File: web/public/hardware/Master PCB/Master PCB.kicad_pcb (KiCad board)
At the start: 2 copper layers, 104 parts, among them J1 SWD Conn, J10 LED3, J11 LDR4, J12 LED4, J13 LED Conn, J2 OLED1, J3 OLED2, J4 5V_IN, J5 LDR1, J6 LED1, J7 LDR2, J8 LED2, J9 LDR3, Q1 2N7000, Q2 2N7000, Q3 2N7000, Q4 2N7000, SW1 nRST, SW2 Menu Encoder, U1 STM32U585VITx, U2 M95P32-IXMNT, U3 TLV62568DBV, U4 LM339

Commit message: Route lots
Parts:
- added C21: 100nF, Capacitor_SMD:C_0805_2012Metric_Pad1.18x1.45mm_HandSolder, F.Cu at (163.5, 106.0)
- U4: footprint Package_DIP:DIP-14_W7.62mm_LongPads -> Package_SO:TSSOP-14_4.4x5mm_P0.65mm
- moved C12 77.9 mm to (141.2, 100.4), turned to -90 degrees
- moved C11 75.7 mm to (143.4, 100.4), turned to -90 degrees
- moved L1 75.3 mm to (152.5, 59.9)
- moved C14 71.0 mm to (154.2, 63.0), turned to -90 degrees
- moved C9 69.8 mm to (150.5, 103.9), turned to 180 degrees
- moved C15 69.7 mm to (156.4, 63.0), turned to -90 degrees
- moved C10 69.6 mm to (150.5, 106.1), turned to 180 degrees
- moved C5 69.3 mm to (145.6, 100.4), turned to -90 degrees
- moved U3 69.1 mm to (150.3, 63.0), turned to 180 degrees
- moved C13 67.1 mm to (146.7, 65.7)
- moved R3 67.0 mm to (144.5, 65.7)
- moved C8 66.7 mm to (148.0, 92.6), turned to 180 degrees
- moved C7 64.1 mm to (151.4, 84.2), turned to 90 degrees
- moved R4 62.8 mm to (149.8, 68.3), turned to 180 degrees
- moved C4 61.6 mm to (147.8, 100.4), turned to -90 degrees
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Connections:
- J1 pad 2: /SWDIO -> /STM32/SWDIO
- J1 pad 3: /SWCLK -> /STM32/SWCLK
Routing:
- net /COL17: track 0.00 -> 42.9 mm
- net /COL1: track 0.00 -> 42.0 mm
- net /COL0: track 0.00 -> 41.0 mm
- net /COL16: track 0.00 -> 40.9 mm
- net /COL19: track 0.00 -> 39.3 mm
- net /COL18: track 0.00 -> 38.1 mm
- net /COL2: track 0.00 -> 36.1 mm
- net /COL21: track 0.00 -> 35.4 mm
- net /COL20: track 0.00 -> 34.6 mm
- net /COL3: track 0.00 -> 32.4 mm
- net /COL23: track 0.00 -> 31.5 mm
- net /COL25: track 0.00 -> 30.4 mm
- net /COL22: track 0.00 -> 30.0 mm
- net +3V3: track 3.30 -> 33.2 mm
- net /COL5: track 0.00 -> 28.4 mm
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- added copper zone on F.Cu, net +3V3
- added copper zone on F.Cu, net Net-(U3-SW)
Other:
- board outline added: 100 x 100 mm
- board text added: "+"
- board text added: "-"
- board text added: "5V"
- board text added: "BOOT0"
- board text added: "C0"
- board text added: "C1"
- board text added: "C10"
- board text added: "C11"
- board text added: "C12"
- board text added: "C13"
- board text added: "C14"
- board text added: "C15"
- board text added: "C16"
- board text added: "C17"
- board text added: "C18"
- board text added: "C19"
- board text added: "C2"
- board text added: "C20"
- board text added: "C21"
- board text added: "C22"
- board text added: "C23"
- board text added: "C24"
- board text added: "C25"
- board text added: "C26"
- board text added: "C27"
- board text added: "C28"
- board text added: "C29"
- board text added: "C3"
- board text added: "C30"
- board text added: "C31"
- board text added: "C4"
- board text added: "C5"
- board text added: "C6"
- board text added: "C7"
- board text added: "C8"
- board text added: "C9"
- board text added: "G"
- board text added: "LDR1"
- board text added: "LDR2"
- board text added: "LDR3"
- board text added: "LDR4"
- board text added: "LED"
- board text added: "RESET"
- board text added: "SWD"

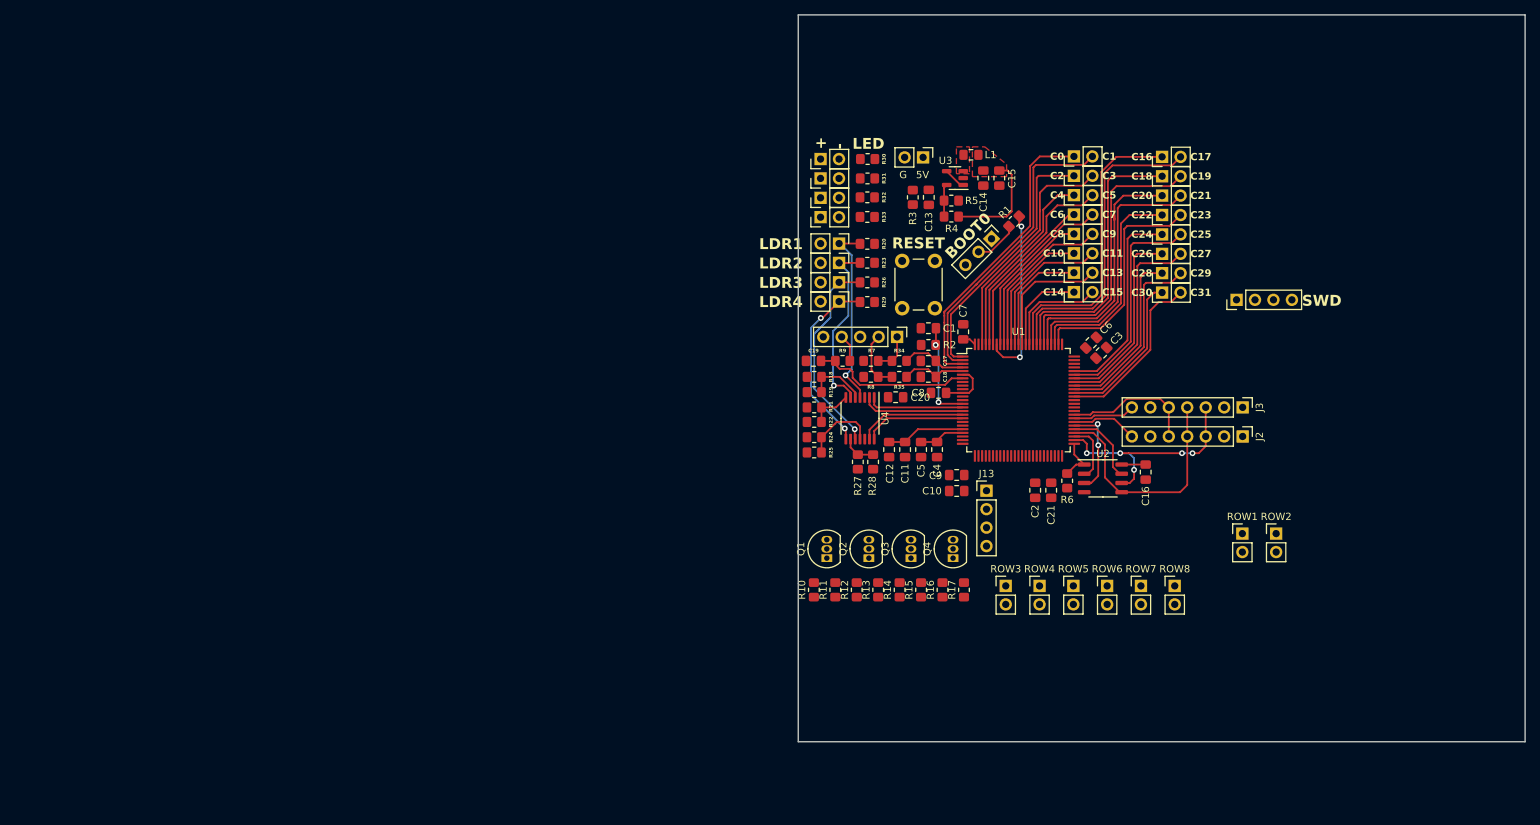
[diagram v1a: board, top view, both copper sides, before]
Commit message: Finish routing Master PCB, create sensor PCB project
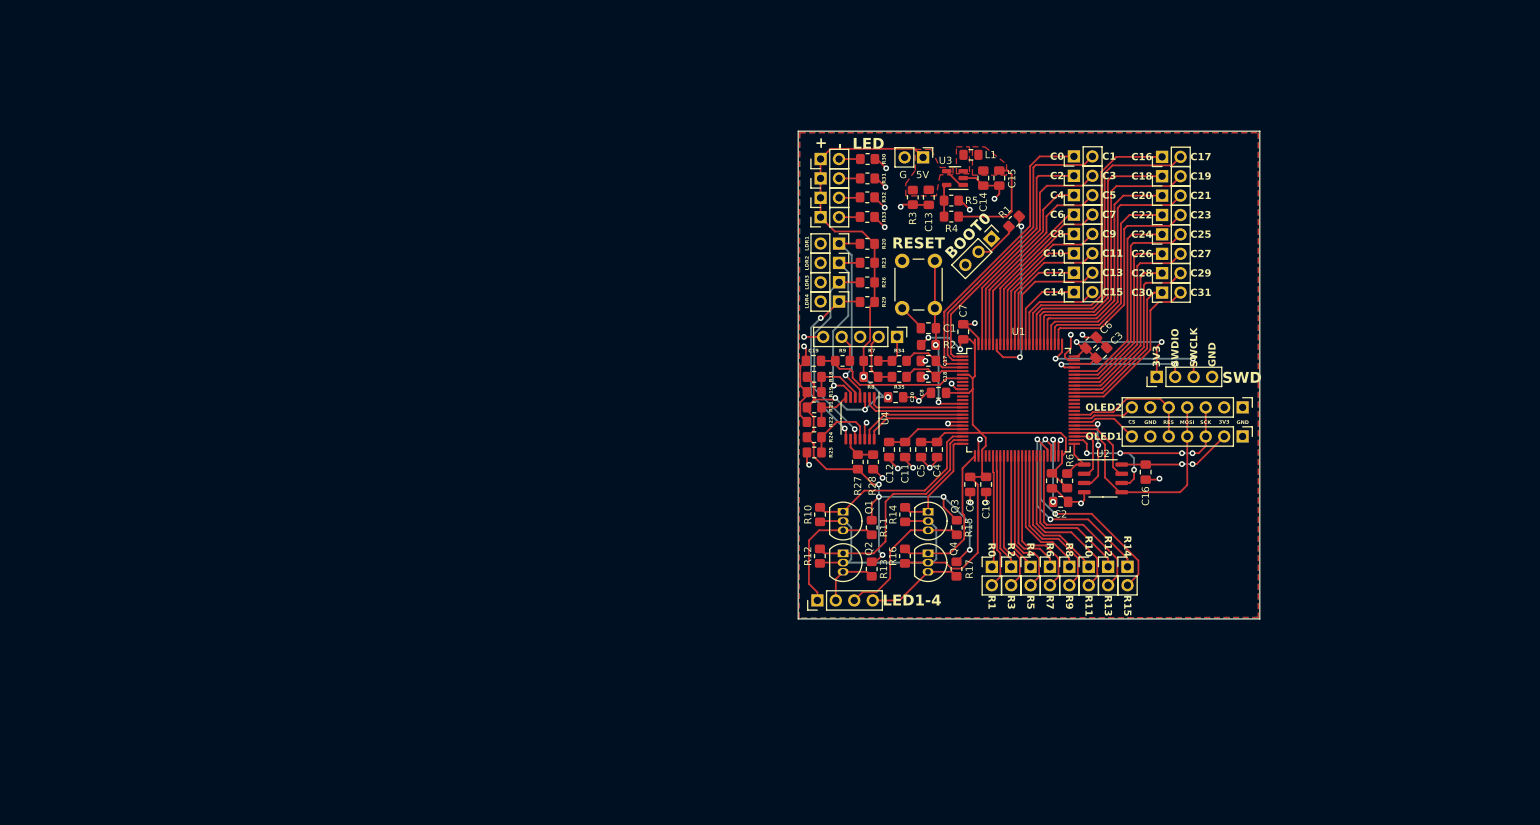
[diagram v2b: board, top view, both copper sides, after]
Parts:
- moved ROW2 36.7 mm to (158.0, 116.5)
- moved ROW1 34.8 mm to (155.3, 116.5)
- moved J13 27.7 mm to (131.3, 121.2), turned to 90 degrees
- moved J1 15.3 mm to (178.0, 90.4)
- moved R10 10.4 mm to (131.7, 109.3)
- moved R14 10.4 mm to (143.4, 109.3)
- moved R11 9.93 mm to (138.8, 111.1), turned to -90 degrees
- moved R15 8.80 mm to (150.5, 111.1), turned to -90 degrees
- moved ROW8 7.01 mm to (174.0, 116.5)
- moved R12 6.87 mm to (131.7, 115.1)
- moved Q3 6.80 mm to (146.6, 109.0), turned to -90 degrees
- moved Q1 6.76 mm to (134.9, 109.0), turned to -90 degrees
- moved ROW7 5.23 mm to (171.3, 116.5)
- moved R16 5.14 mm to (143.4, 115.1)
- moved ROW3 4.31 mm to (160.7, 116.5)
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- renumbered R16 to R15, R15 to R16
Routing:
- net +3V3: track 33.2 -> 180.6 mm, vias 0 -> 6
- net +5V: track 3.07 -> 136.4 mm, vias 0 -> 9
- net GND: track 0.00 -> 96.4 mm, vias 0 -> 29
- net /ROW15: track 0.00 -> 32.1 mm, vias 0 -> 2
- net /LED/LED2IN: track 0.00 -> 31.7 mm
- net /ROW14: track 0.00 -> 28.5 mm, vias 0 -> 2
- net /LED/LED1IN: track 0.00 -> 26.3 mm
- net /ROW13: track 0.00 -> 25.4 mm
- net /ROW11: track 0.00 -> 23.9 mm
- net /STM32/SWCLK: track 0.00 -> 23.8 mm, vias 0 -> 2
- net /ROW9: track 0.00 -> 22.3 mm
- net /ROW7: track 0.00 -> 21.9 mm
- net /ROW12: track 0.00 -> 21.7 mm
- net /LED/LED4IN: track 0.00 -> 21.5 mm
- net /LED/LED3OUT: track 0.00 -> 20.6 mm
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- added copper zone on F.Cu, net +5V
- added copper zone on B.Cu, net GND
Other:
- board size 100 x 100 mm -> 63.5 x 67.1 mm
- board text added: "3V3"
- board text added: "CS"
- board text added: "GND"
- board text added: "LED1-4"
- board text added: "MOSI"
- board text added: "OLED1"
- board text added: "OLED2"
- board text added: "R0"
- board text added: "R1"
- board text added: "R10"
- board text added: "R11"
- board text added: "R12"
- board text added: "R13"
- board text added: "R14"
- board text added: "R15"
- board text added: "R2"
- board text added: "R3"
- board text added: "R4"
- board text added: "R5"
- board text added: "R6"
- board text added: "R7"
- board text added: "R8"
- board text added: "R9"
- board text added: "RES"
- board text added: "SCK"
- board text added: "SWCLK"
- board text added: "SWDIO"

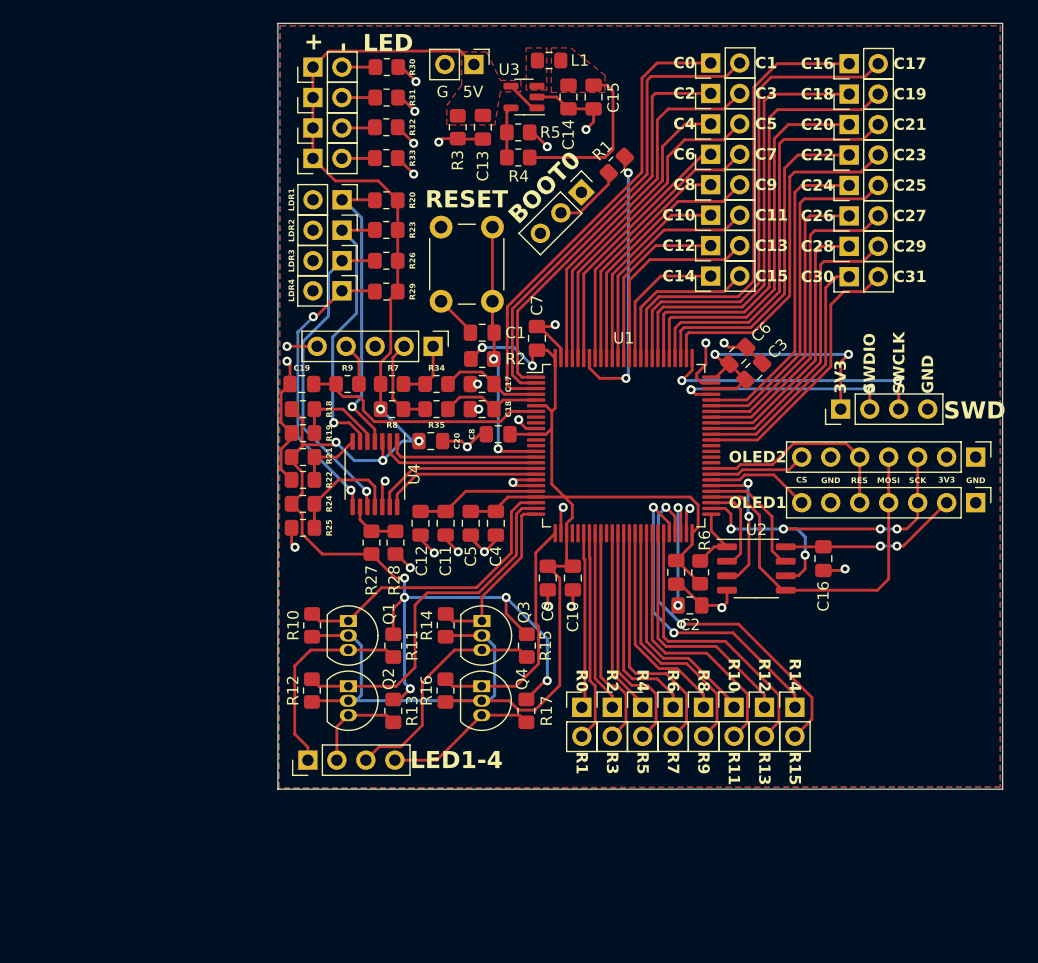
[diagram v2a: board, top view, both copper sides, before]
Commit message: Add missing signals to master PCB for relay and OLED DC, add mounting holes, add text, add dimensions
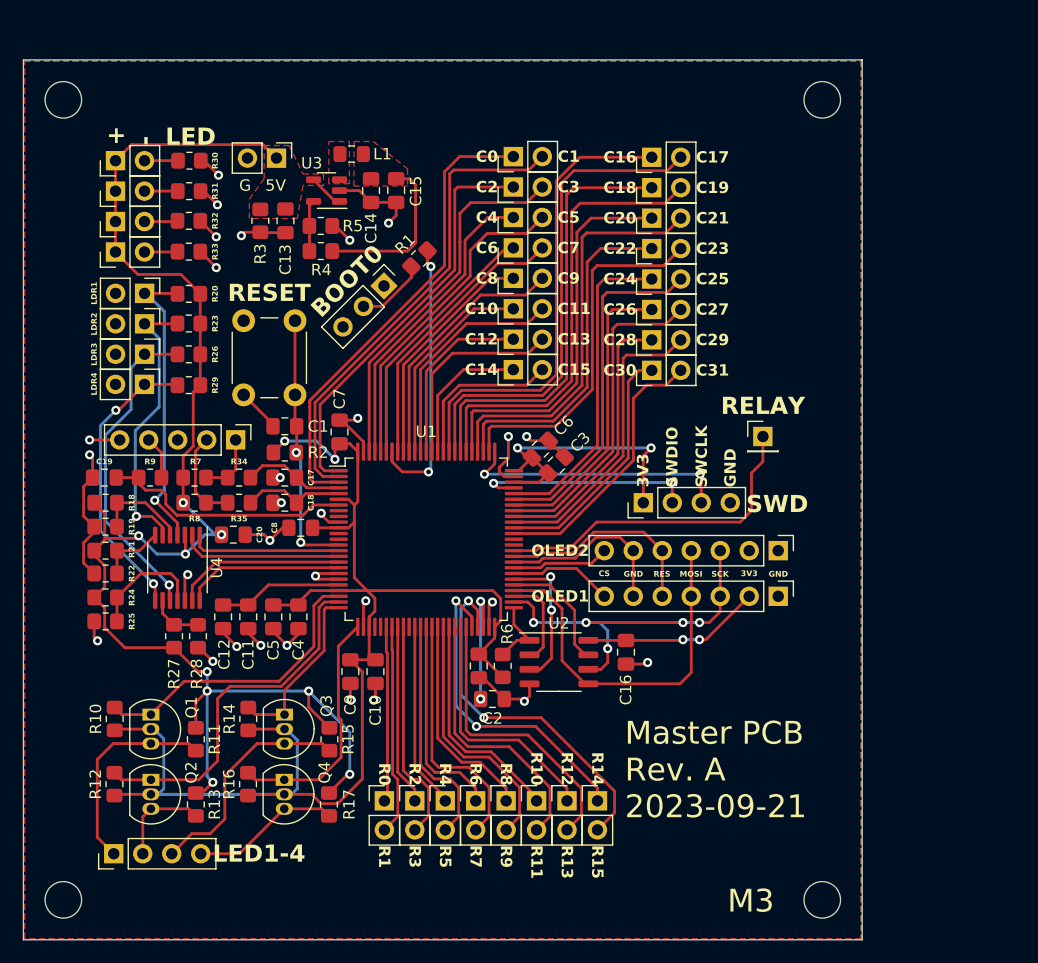
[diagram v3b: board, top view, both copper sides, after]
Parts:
- added H1: MountingHole, MountingHole:MountingHole_3.2mm_M3, F.Cu at (109.9, 63.3)
- added H2: MountingHole, MountingHole:MountingHole_3.2mm_M3, F.Cu at (176.4, 63.3)
- added H3: MountingHole, MountingHole:MountingHole_3.2mm_M3, F.Cu at (109.9, 133.4)
- added H4: MountingHole, MountingHole:MountingHole_3.2mm_M3, F.Cu at (176.4, 133.4)
- added J14: Relay Conn, Connector_PinHeader_2.54mm:PinHeader_1x01_P2.54mm_Vertical, F.Cu at (171.2, 92.8)
- moved C10 19.1 mm to (137.2, 113.4)
- moved C15 19.1 mm to (139.1, 71.2)
- moved C16 19.1 mm to (159.2, 111.7)
- moved C19 19.1 mm to (113.5, 96.4)
- moved C2 19.1 mm to (147.5, 115.8)
- moved C3 19.1 mm to (153.1, 95.3)
- moved C6 19.1 mm to (151.7, 93.9)
- moved C7 19.1 mm to (134.1, 92.4)
- moved C8 19.1 mm to (130.7, 100.8)
- moved J10 19.1 mm to (114.5, 74.0)
- moved J12 19.1 mm to (114.5, 76.6)
- moved J2 19.1 mm to (172.5, 106.8)
- moved J3 19.1 mm to (172.5, 102.8)
- moved J4 19.1 mm to (128.6, 68.4)
- moved J5 19.1 mm to (117.0, 80.3)
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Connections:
- J2 pad 6: GND -> /OLED1DC
- J3 pad 6: GND -> /OLED1DC
- U1 pad 12: unconnected-(U1-PH0-Pad12) -> /STM32/OSC_IN
- U1 pad 13: unconnected-(U1-PH1-Pad13) -> /STM32/OSC_OUT
- U1 pad 59: /OLEDRES -> /OLED1DC
- U1 pad 60: unconnected-(U1-PD13-Pad60) -> /OLEDRES
- U1 pad 61: unconnected-(U1-PD14-Pad61) -> /STM32/RELAY
- U1 pad 8: unconnected-(U1-PC14-Pad8) -> /STM32/OSC32_IN
- U1 pad 9: unconnected-(U1-PC15-Pad9) -> /STM32/OSC32_OUT
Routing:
- net /STM32/RELAY: track 0.00 -> 29.2 mm
- net /OLED1DC: track 0.00 -> 15.9 mm
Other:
- board size 63.5 x 67.1 mm -> 73.5 x 77.1 mm
- board text added: "M3"
- board text added: "Master PCB Rev. A 2023-09-21"
- board text added: "RELAY"

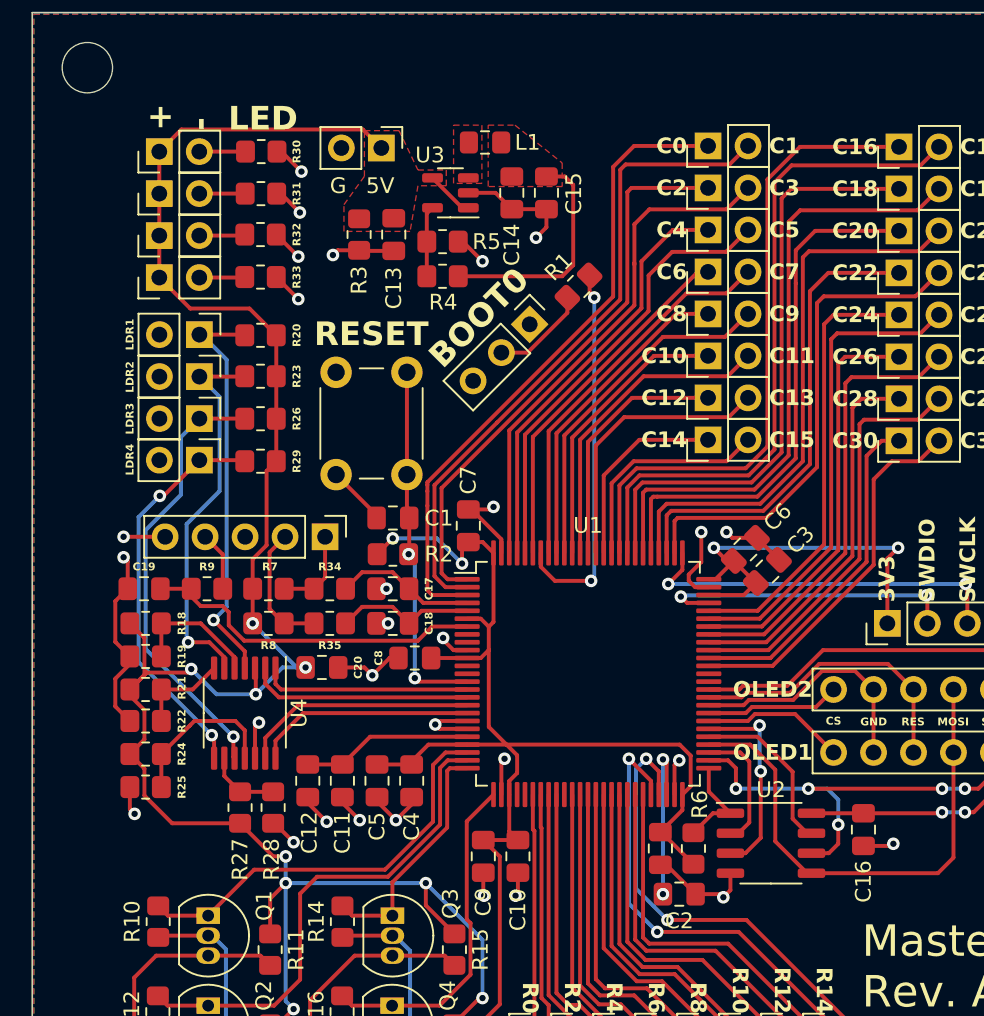
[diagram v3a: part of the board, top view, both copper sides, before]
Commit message: Add 5V power trace to master PCB
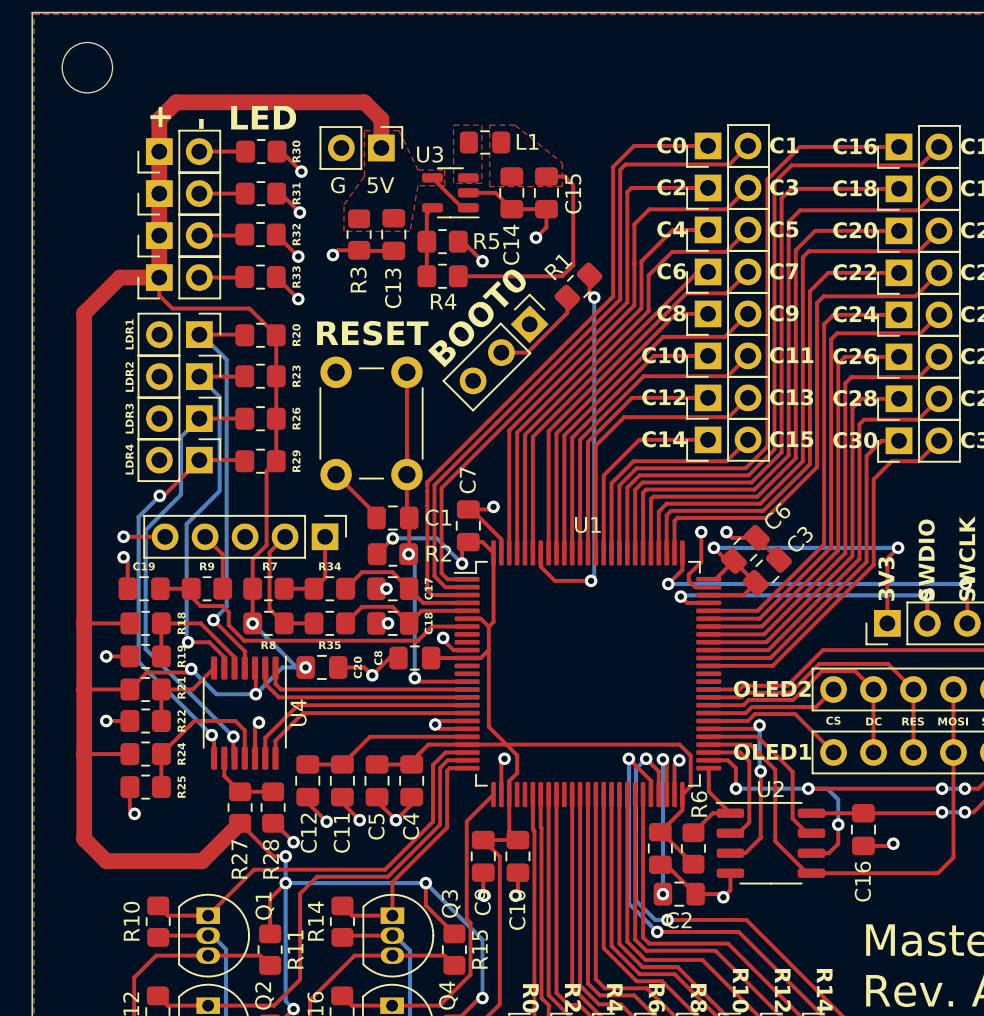
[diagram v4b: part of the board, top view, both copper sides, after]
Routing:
- net +5V: track 136.4 -> 180.4 mm
- net GND: track 96.4 -> 89.5 mm, vias 29 -> 31
- net /STM32/nRST: track 23.9 -> 23.1 mm
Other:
- board text added: "DC"
